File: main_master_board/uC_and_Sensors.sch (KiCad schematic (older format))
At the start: 3 parts, among them U1 NRF24L01+, U15 DSPIC33EP512GP806-I/PT, U16 DWM1000

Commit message: Started hooking up the dsPIC uC
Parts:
- removed U15: DSPIC33EP512GP806-I/PT, dp_devices:dp_devices-TQFP-64-10X10, symbol DSPIC33EP512GP806-I/PT
- added C? (x5): 100nF, symbol C_Small
- added C?: 10uF, symbol C_Small
- added C?: C, symbol C
- added C?: 10uF, symbol C
- added C?: 100nF, symbol C
- added D?: DA2S10100L, SSMini2-F5-B:SSMini2-F5-B, symbol D_Small
- added L?: MCSMT-G5030A1-3712, symbol MCSMT-G5030A1-3712
- added R? (x2): R, symbol R
- added R?: 50, symbol R
- added U?: DSPIC33EP512GP806-I/PT, symbol DSPIC33EP512GP806-I/PT
- added U?: Si1900DL, MODULE, symbol Si1900DL
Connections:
- net labels added: KS_uC, PGEC1, PGED1, RF_CE, RF_CSN, RF_GND, RF_IRQ, RF_MISO, RF_MOSI, RF_SCK, buzz_gnd, buzzer, ks_nFault_signal, mclr_gnd, reset_dsPIC, uC_KS_1, uC_KS_2, vmotor_en_signal, ~MCLR
- wire segments 6 -> 119
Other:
- moved on the sheet: U1, U16

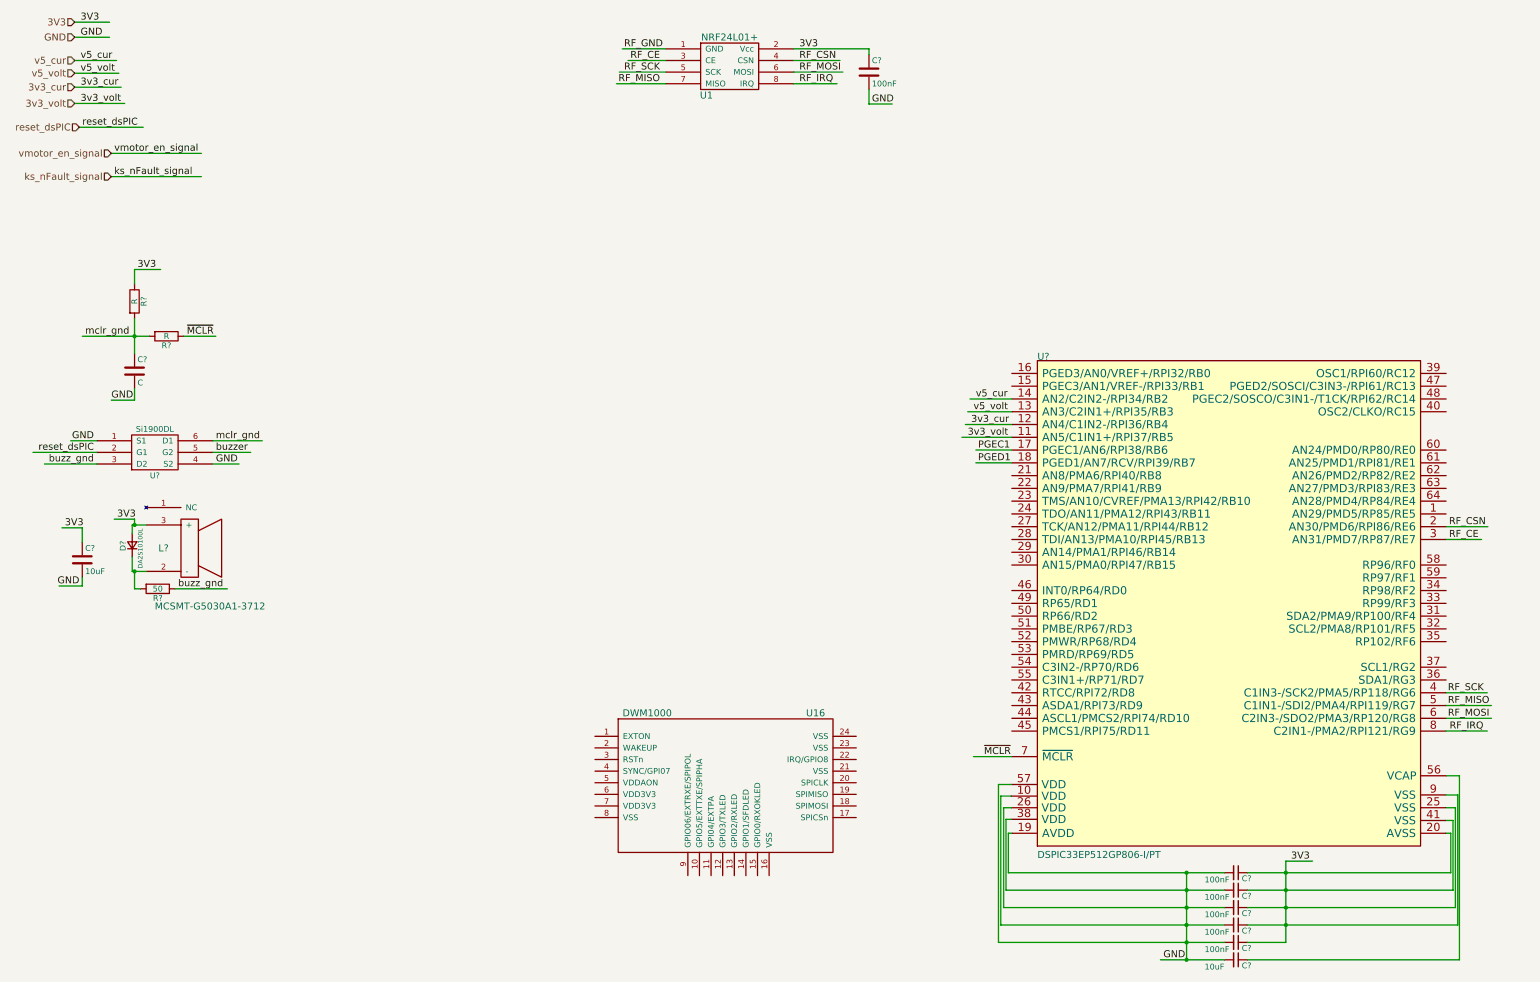
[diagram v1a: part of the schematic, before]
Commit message: Started adding support for a new snapdragon board. Dart0410
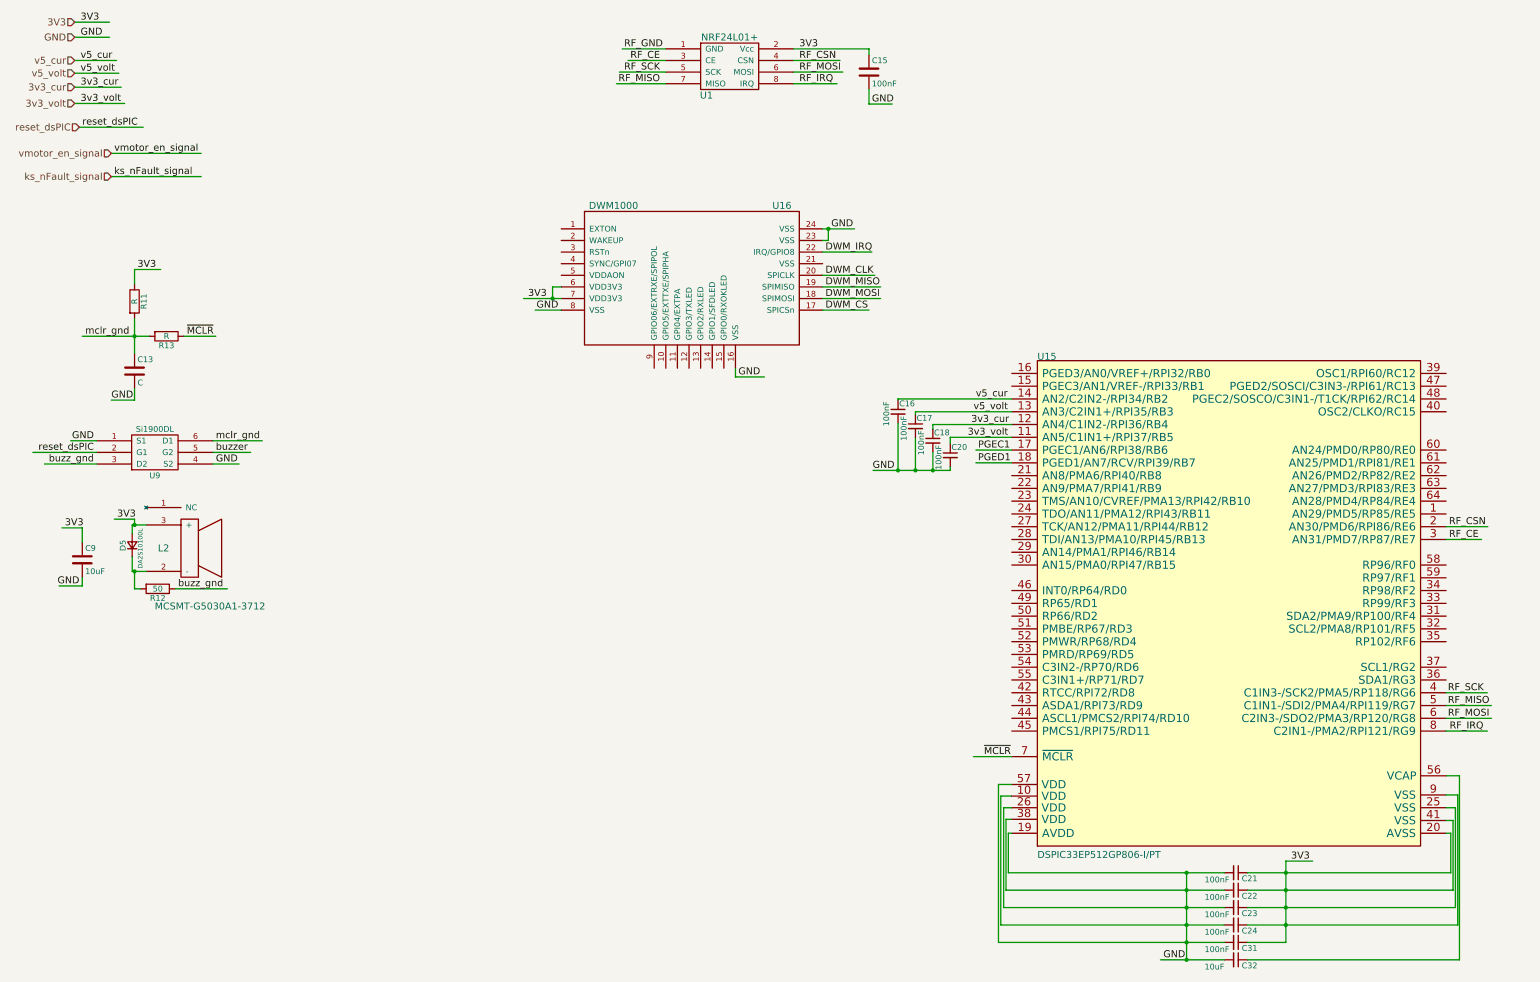
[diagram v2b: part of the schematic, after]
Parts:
- added C16, C17, C18, C20: 100nF, symbol C_Small
- U15: renamed from U?; footprint (none) -> dp_devices:dp_devices-TQFP-64-10X10
- U9: renamed from U?; footprint MODULE -> NASA_IRG_SSB:SOT323-6
- gave numbers to parts that had none: 14
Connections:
- net labels added: DWM_CLK, DWM_CS, DWM_IRQ, DWM_MISO, DWM_MOSI
- wire segments 119 -> 121
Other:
- moved on the sheet: U16

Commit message: Lots of stuff
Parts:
- added D16, D7: LED, LEDs:LED_0603, symbol LED
- added P14, P15: CONN_01X04, microclasp_4:microclasp_4, symbol CONN_01X04
- added R14, R15: 470, Resistors_SMD:R_0603, symbol R
- added R16, R23: 1K, Resistors_SMD:R_0603, symbol R
- C13: value C -> 100nF; footprint (none) -> Capacitors_SMD:C_0603
- C15, C16, C17, C18, C20, C21, C22, C23, C24, C31, C32, C9: footprint (none) -> Capacitors_SMD:C_0603
- L2: footprint (none) -> MCSMT-G5030A1-3712:MCSMT-G5030A1-3712
- R11: value R -> 10k; footprint (none) -> Resistors_SMD:R_0603
- R12: footprint (none) -> Resistors_SMD:R_0603
- R13: value R -> 470; footprint (none) -> Resistors_SMD:R_0603
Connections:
- net labels added: RESET, RXXLED, TXLED, WAKEUP, prog_UART_RX, prog_UART_TX, prog_~UART_CTS, prog_~UART_RTS, uC_SCL, uC_SDA
- wire segments 121 -> 163
- no-connect marks 0 -> 7
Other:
- note added: "AMS5600 Magnetic Rotary \nSensor Support\n"
- note added: "TCS3472 Color Sensor Support\n"
- moved on the sheet: C15, U1, U16

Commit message: Working on moving things to two boards
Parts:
- removed P14, P15: CONN_01X04, microclasp_4:microclasp_4, symbol CONN_01X04
- D16, D7: symbol LED -> LED-RESCUE-main_master_board
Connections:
- wire segments 163 -> 157
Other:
- note removed: "AMS5600 Magnetic Rotary \nSensor Support\n"
- note removed: "TCS3472 Color Sensor Support\n"
- moved on the sheet: R16, R23
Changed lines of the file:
@@
 LIBS:FDS4935A
 LIBS:Si1900DL
-LIBS:Amplifiers
-LIBS:Connectors
-LIBS:DataStorage
-LIBS:Diodes
-LIBS:Microprocessors
-LIBS:MiscellaneousDevices
-LIBS:Passives
-LIBS:PMOD
-LIBS:PowerComponents
-LIBS:RepeaterParts
-LIBS:RF_OEM_Parts
 LIBS:Sensors
-LIBS:TransistorParts
 LIBS:LP3852-3.3
 LIBS:0s102011ma1qn1
@@
 LIBS:xal5050-562meb
 LIBS:xal6030-182mec
-LIBS:decaWave
 LIBS:conn_2x50
 LIBS:conn_open_q_x2
@@
 LIBS:ac-dc
 LIBS:actel
-LIBS:allegro
 LIBS:Altera
 LIBS:analog_devices
@@
 LIBS:logo
 LIBS:maxim
-LIBS:mechanical
 LIBS:microchip_dspic33dsc
 LIBS:microchip_pic10mcu
@@
 LIBS:microchip_pic32mcu
 LIBS:motor_drivers
-LIBS:motors
 LIBS:msp430
 LIBS:nordicsemi
@@
 LIBS:ttl_ieee
 LIBS:video
-LIBS:wiznet
 LIBS:Worldsemi
 LIBS:Xicor
-LIBS:zetex
 LIBS:Zilog
 LIBS:conn_2x45
@@
 NoConn ~ 9200 1975
 $Comp
-L LED D7
+L LED-RESCUE-main_master_board D7
 U 1 1 587FD80A
 P 9775 2350
+AR Path="/587FD80A" Ref="D7"  Part="1"
+AR Path="/5878C64D/587FD80A" Ref="D7"  Part="1"
 F 0 "D7" H 9775 2450 50  0000 C CNN
 F 1 "LED" H 9775 2250 50  0000 C CNN
@@
 $EndComp
 $Comp
-L LED D16
+L LED-RESCUE-main_master_board D16
 U 1 1 587FDA5E
 P 9775 2625
+AR Path="/587FDA5E" Ref="D16"  Part="1"
+AR Path="/5878C64D/587FDA5E" Ref="D16"  Part="1"
 F 0 "D16" H 9775 2725 50  0000 C CNN
 F 1 "LED" H 9775 2525 50  0000 C CNN
@@
 uC_SDA
 Wire Wire Line
-	12870 6225 13225 6225
-Wire Wire Line
-	12870 6335 13230 6335
-$Comp
-L CONN_01X04 P15
-U 1 1 5880D5C7
-P 12875 1175
-F 0 "P15" H 12875 1425 50  0000 C CNN
-F 1 "CONN_01X04" V 12975 1175 50  0000 C CNN
-F 2 "microclasp_4:microclasp_4" H 12875 1175 50  0001 C CNN
-F 3 "" H 12875 1175 50  0000 C CNN
-	1    12875 1175
-	1    0    0    -1
-$EndComp
-Wire Wire Line
-	12675 1025 12450 1025
-Text Label 12650 1025 2    60   ~ 0
-GND
-Text Label 12650 1125 2    60   ~ 0
-3V3
-Wire Wire Line
-	12675 1125 12475 1125
-Text Label 12650 1225 2    60   ~ 0
-uC_SCL
-Text Label 12650 1325 2    60   ~ 0
-uC_SDA
-Wire Wire Line
-	12100 1225 12675 1225
-Wire Wire Line
-	11925 1325 12675 1325
+	13700 6225 12870 6225
+Wire Wire Line
+	13875 6335 12870 6335
 $Comp
 L R R23
 U 1 1 58810FC4
-P 12100 1050
-F 0 "R23" V 12180 1050 50  0000 C CNN
-F 1 "1K" V 12100 1050 50  0000 C CNN
-F 2 "Resistors_SMD:R_0603" V 12030 1050 50  0001 C CNN
-F 3 "" H 12100 1050 50  0000 C CNN
-	1    12100 1050
-	1    0    0    -1
+P 13700 6025
+F 0 "R23" V 13780 6025 50  0000 C CNN
+F 1 "1K" V 13700 6025 50  0000 C CNN
+F 2 "Resistors_SMD:R_0603" V 13630 6025 50  0001 C CNN
+F 3 "" H 13700 6025 50  0000 C CNN
+	1    13700 6025
+	-1   0    0    -1
 $EndComp
 $Comp
 L R R16
 U 1 1 58811199
-P 11925 1050
-F 0 "R16" V 12005 1050 50  0000 C CNN
-F 1 "1K" V 11925 1050 50  0000 C CNN
-F 2 "Resistors_SMD:R_0603" V 11855 1050 50  0001 C CNN
-F 3 "" H 11925 1050 50  0000 C CNN
-	1    11925 1050
-	1    0    0    -1
-$EndComp
-Wire Wire Line
-	12100 1200 12100 1225
-Wire Wire Line
-	11925 1325 11925 1200
-Wire Wire Line
-	11925 900  11925 850
-Wire Wire Line
-	11925 850  12100 850
-Wire Wire Line
-	12100 850  12100 900
-Text Label 11950 850  0    60   ~ 0
+P 13875 6025
+F 0 "R16" V 13955 6025 50  0000 C CNN
+F 1 "1K" V 13875 6025 50  0000 C CNN
+F 2 "Resistors_SMD:R_0603" V 13805 6025 50  0001 C CNN
+F 3 "" H 13875 6025 50  0000 C CNN
+	1    13875 6025
+	-1   0    0    -1
+$EndComp
+Wire Wire Line
+	13700 6175 13700 6225
+Wire Wire Line
+	13875 6175 13875 6335
+Wire Wire Line
+	13875 5875 13875 5825
+Wire Wire Line
+	13875 5825 13700 5825
+Wire Wire Line
+	13700 5825 13700 5875
+Text Label 13850 5825 2    60   ~ 0
 3V3
-Text Notes 11950 725  0    60   ~ 0
-AMS5600 Magnetic Rotary \nSensor Support\n
-$Comp
-L CONN_01X04 P14
-U 1 1 58814DFF
-P 12850 1875
-F 0 "P14" H 12850 2125 50  0000 C CNN
-F 1 "CONN_01X04" V 12950 1875 50  0000 C CNN
-F 2 "microclasp_4:microclasp_4" H 12850 1875 50  0001 C CNN
-F 3 "" H 12850 1875 50  0000 C CNN
-	1    12850 1875
-	1    0    0    -1
-$EndComp
-Wire Wire Line
-	12650 1725 12425 1725
-Text Label 12625 1725 2    60   ~ 0
-GND
-Text Label 12625 1825 2    60   ~ 0
-3V3
-Wire Wire Line
-	12650 1825 12450 1825
-Text Label 12625 1925 2    60   ~ 0
-uC_SCL
-Text Label 12625 2025 2    60   ~ 0
-uC_SDA
-Wire Wire Line
-	12650 1925 12300 1925
-Wire Wire Line
-	12650 2025 12300 2025
-Text Notes 11825 1550 0    60   ~ 0
-TCS3472 Color Sensor Support\n
 Text HLabel 1350 2275 0    60   Input ~ 0
 prog_UART_RX
@@
 Wire Wire Line
 	1350 2650 1950 2650
+Text HLabel 15400 1350 2    60   Output ~ 0
+uC_SDA
+Text HLabel 15400 1475 2    60   Output ~ 0
+uC_SCL
+Wire Wire Line
+	15400 1350 15050 1350
+Text Label 15375 1350 2    60   ~ 0
+uC_SDA
+Text Label 15375 1475 2    60   ~ 0
+uC_SCL
+Wire Wire Line
+	15400 1475 15050 1475
 $EndSCHEMATC

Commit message: Added a lot of things. Put a 5v to 4v buck as well as supporing the snapdragon board
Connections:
- net labels added: RB0, RB1, RB10, RB11, RB12, RB8, RB9, RD1, RD10, RD11, RD2, RD3, RD4, RD5, RD6, RD9, RE5, RF2, RF3, RF4, RF5, RF6, sensor_SCL, sensor_SDA, uC_CLK, uC_CS, uC_GPIO1, uC_GPIO2, uC_MISO, uC_MOSI, uC_UART_RX, uC_UART_TX
- net labels removed: prog_~UART_CTS, prog_~UART_RTS
- wire segments 157 -> 191
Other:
- note added: "uC_Slave SPI"
- moved on the sheet: C13, C9, D5, L2, R11, R12, R13, U9

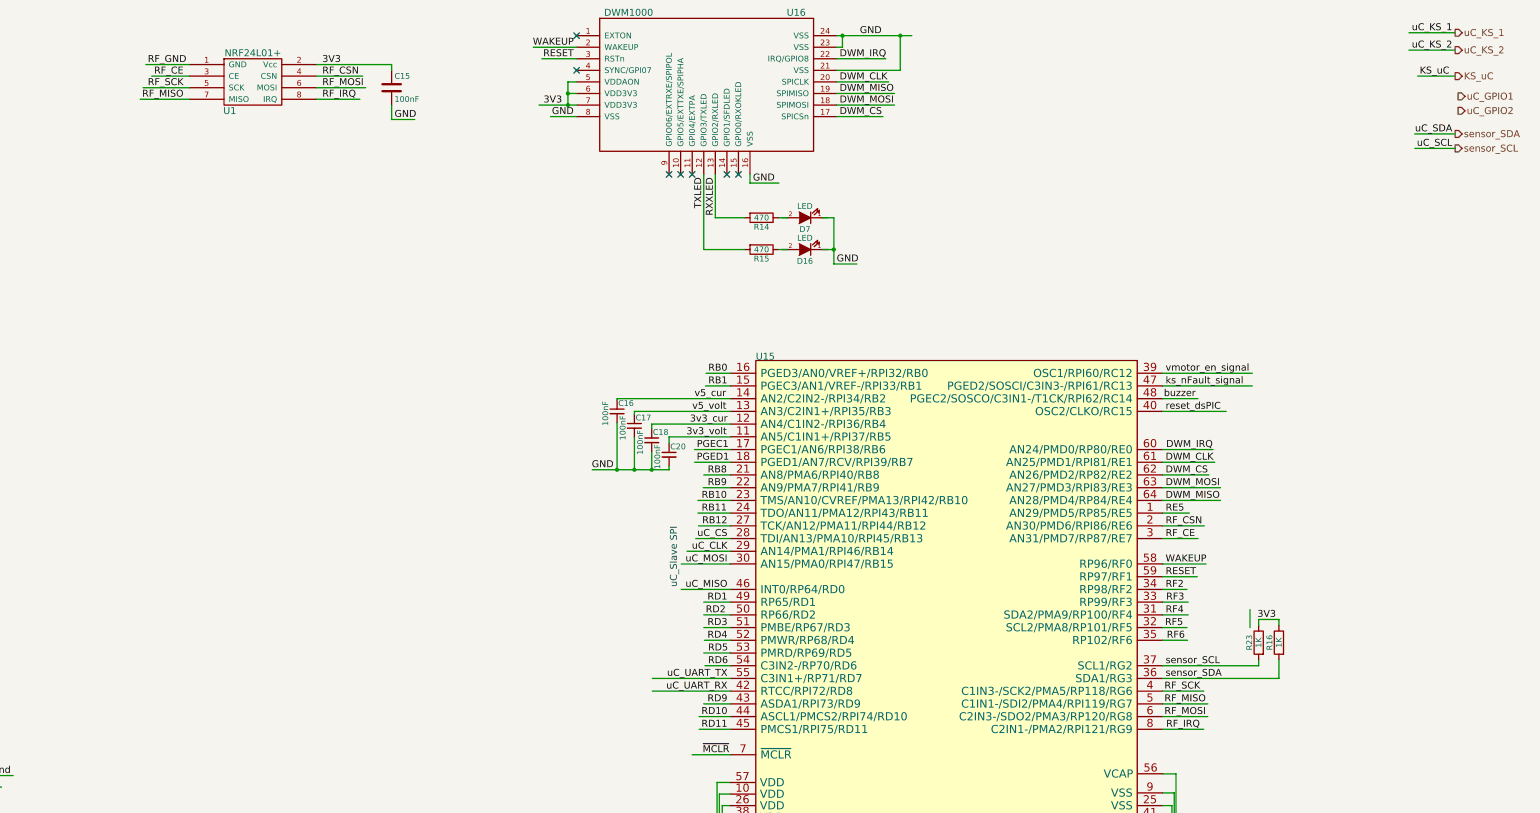
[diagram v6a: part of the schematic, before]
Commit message: Cleaned up some wires and moved connectors out to main page. Also added some LEDs
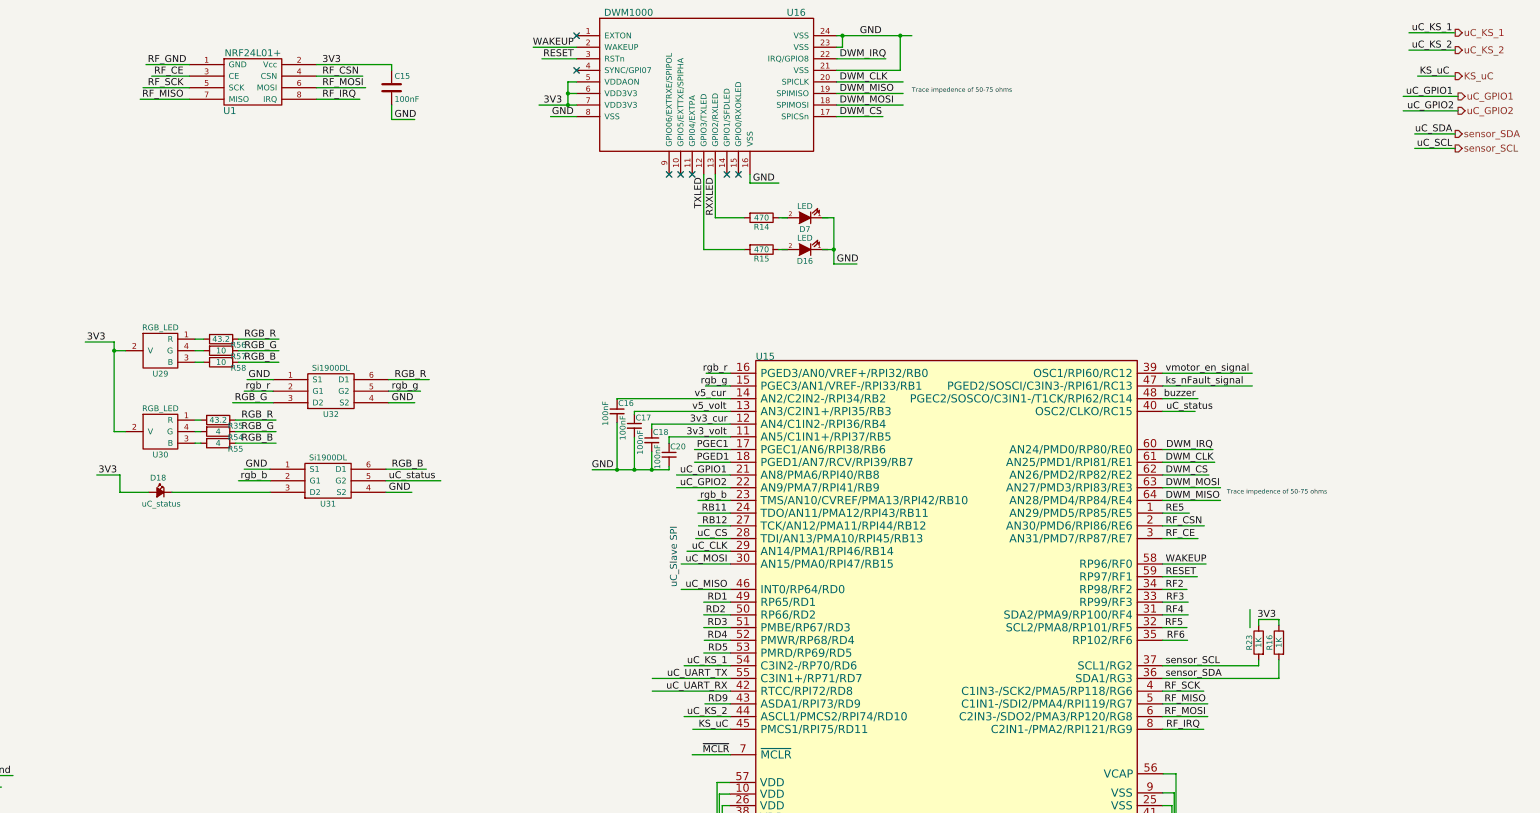
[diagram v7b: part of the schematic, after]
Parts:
- added D18: uC_status, LEDs:LED_0603, symbol Led_Small
- added R35, R56: 43.2, Resistors_SMD:R_0603, symbol R
- added R54, R55: 4, Resistors_SMD:R_0603, symbol R
- added R57, R58: 10, Resistors_SMD:R_0603, symbol R
- added U29, U30: RGB_LED, Kingbright:APFA2507QBDSEEZGKC, symbol RGB_LED
- added U31, U32: Si1900DL, NASA_IRG_SSB:SOT323-6, symbol Si1900DL
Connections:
- net labels added: RGB_B, RGB_G, RGB_R, rgb_b, rgb_g, rgb_r, uC_status
- net labels removed: RB0, RB1, RB10, RB8, RB9, RD10, RD11, RD6
- wire segments 191 -> 224
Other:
- note added: "Trace impedence of 50-75 ohms"
